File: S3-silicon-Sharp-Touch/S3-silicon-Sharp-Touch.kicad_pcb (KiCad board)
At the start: 4 copper layers, 77.9 x 45.2 mm, 66 parts, among them IC1 ESP32-S3FN8, J1 USB_C_Receptacle_USB2.0, J2 Conn_01x06_Socket, J3 Conn_01x11_Socket, J4 SM04B-SRSS-TB_LF__SN_, J5 FH52-10S-0.5SH_99, J6 5024260810, J7 S2B-PH-SM4-TB_LF__SN_, Q1 MMBT3904, Q2 MMBT3904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

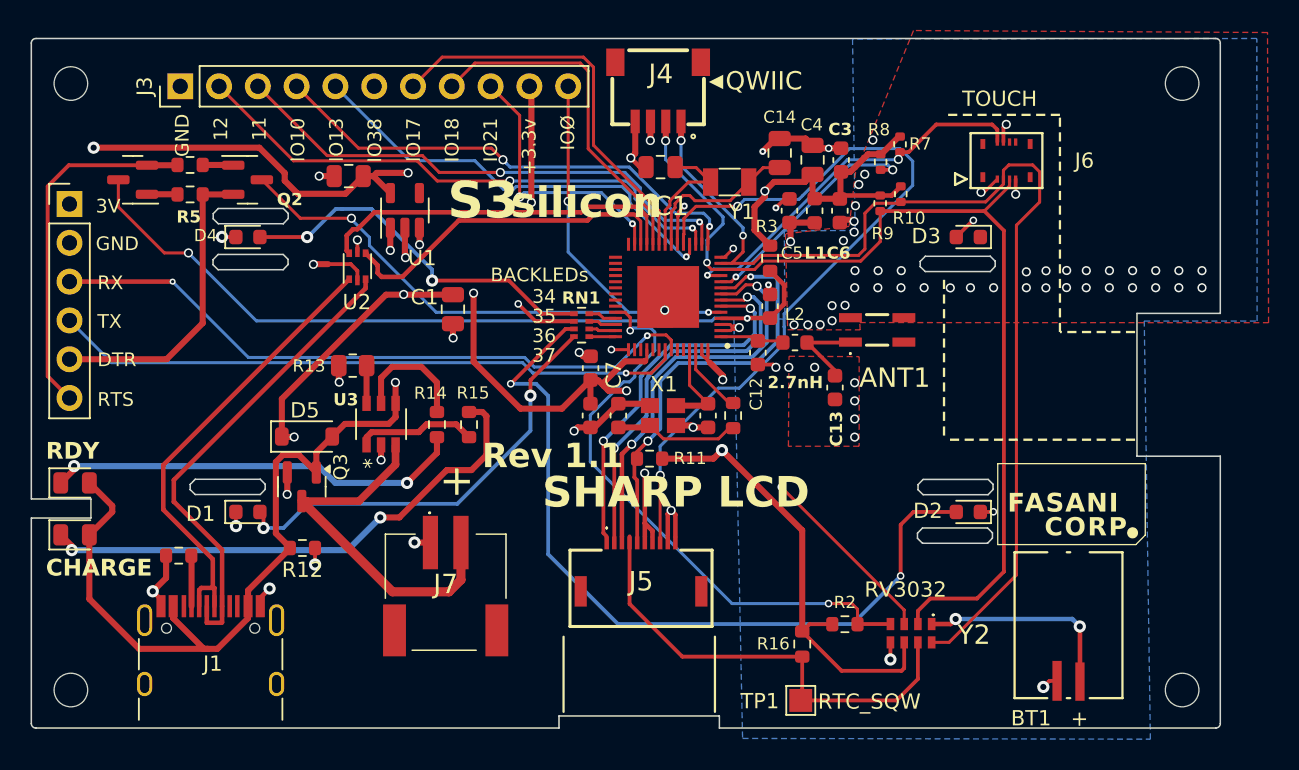
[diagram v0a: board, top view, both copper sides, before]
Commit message: Add U4:Accelerometer
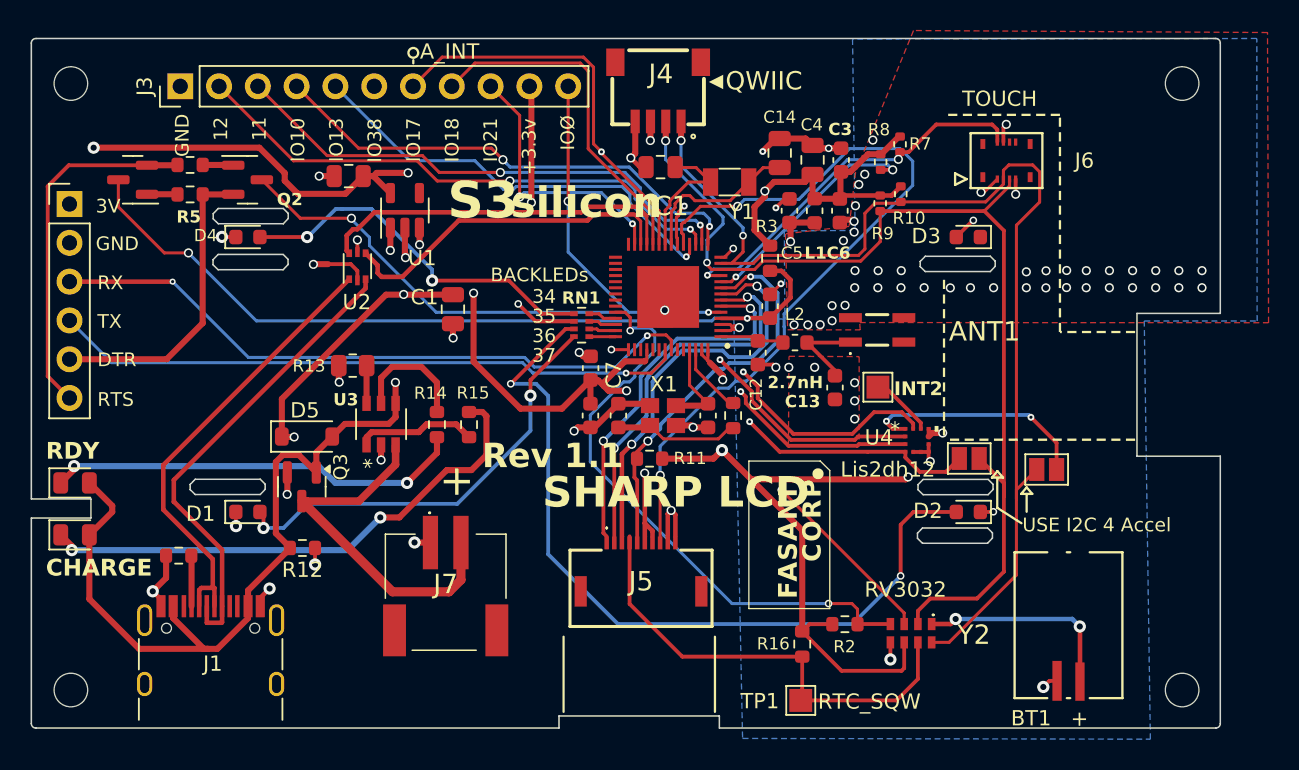
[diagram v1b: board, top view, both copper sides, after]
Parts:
- added JP1: Jumper SDA, Jumper:SolderJumper-2_P1.3mm_Open_Pad1.0x1.5mm, F.Cu at (89.1, 58.5)
- added JP2: Jumper SCL, Jumper:SolderJumper-2_P1.3mm_Open_Pad1.0x1.5mm, F.Cu at (94.1, 59.2)
- added TP2: RTC_INT, TestPoint:TestPoint_Pad_1.5x1.5mm, F.Cu at (83.1, 53.8)
- added U4: LIS2DH12TR, footprints:LIS2DH12TR_LGA-12_STM_Accel, F.Cu at (85.6, 57.3)
- moved G*** 11.0 mm to (66.6, 48.7)
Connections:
- net /IO10 renamed /A_SPI_MOSI
- net /IO11 renamed /A_SPI_CS
- net /IO13 renamed /A_SPI_MISO
- net /IO17 renamed /A_SPI_INT1
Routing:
- net /A_SPI_INT1: track 26.3 -> 63.0 mm, vias 0 -> 2
- net /A_SPI_MOSI: track 32.5 -> 66.4 mm, vias 2 -> 3
- net /A_SPI_CS: track 34.5 -> 58.8 mm, vias 2 -> 3
- net /A_SPI_MISO: track 29.0 -> 52.6 mm, vias 1 -> 2
- net VDD33: track 191.5 -> 207.8 mm, vias 11 -> 13
- net Net-(JP2-B): track 0.00 -> 15.3 mm, vias 0 -> 2
- net Net-(U4-INT2): track 0.00 -> 4.16 mm
- net /SDA: track 67.1 -> 70.2 mm
- net GND: track 49.4 -> 51.9 mm
- net /SCL: track 71.2 -> 73.7 mm
- net /LCD_DISPON: track 27.8 -> 25.6 mm
- net /CHIP_PU: track 53.5 -> 54.3 mm
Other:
- board text added: "A_INT"
- board text added: "INT2"
- board text added: "Lis2dh12"
- board text added: "TOUCH BITCH IO - - - - - 7 SCL I2C 8 SDA I2C 5 REST 6 IRQ (Int)"
- board text added: "USE I2C 4 Accel"
- board text removed: "TOUCH BITCH IO - - - - - 7 SCL I2C 8 SDA I2C 5 REST 6 IRQ (Interrupt)"

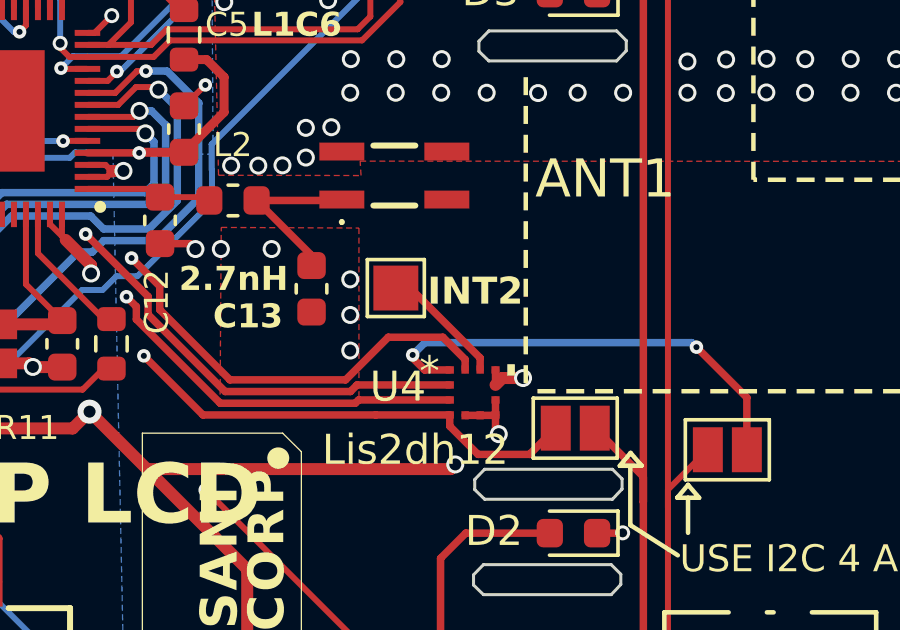
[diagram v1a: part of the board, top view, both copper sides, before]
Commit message: Add pullup to int1 (Accel)
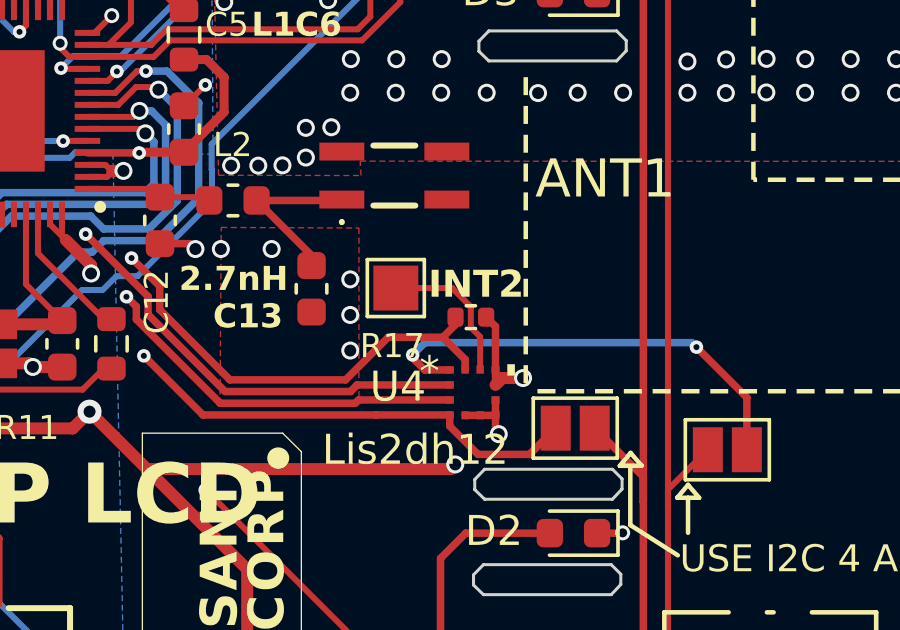
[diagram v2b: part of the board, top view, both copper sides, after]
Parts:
- added R17: 100k, Resistor_SMD:R_0402_1005Metric, F.Cu at (85.6, 54.8)
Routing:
- net VDD33: track 207.8 -> 209.6 mm
- net Net-(U4-INT2): track 4.16 -> 4.98 mm
- net /A_SPI_INT1: track 63.0 -> 63.6 mm
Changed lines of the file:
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@@
       (net 91 "Net-(JP2-B)") (pinfunction "B") (pintype "passive"))
   )
+  (footprint "Resistor_SMD:R_0402_1005Metric" (layer "F.Cu")
+    (at 85.58 54.8)
+    (descr "Resistor SMD 0402 (1005 Metric), square (rectangular) end terminal, IPC_7351 nominal, (Body size source: IPC-SM-782 page 72, https://www.pcb-3d.com/wordpress/wp-content/uploads/ipc-sm-782a_amendment_1_and_2.pdf), generated with kicad-footprint-generator")
+    (tags "resistor")
+    (property "LCSC" "C208960")
+    (property "Sheetfile" "S3-silicon-Sharp-Touch.kicad_sch")
+    (property "Sheetname" "")
+    (property "ki_description" "Resistor")
+    (property "ki_keywords" "R res resistor")
+    (attr smd)
+    (fp_text reference "R17" (at -2.62 0.96) (layer "F.SilkS")
+        (effects (font (size 0.8 0.8) (thickness 0.15)))
+    )
+    (fp_text value "100k" (at 0 1.17) (layer "F.Fab")
+        (effects (font (size 1 1) (thickness 0.15)))
+    )
+    (fp_text user "${REFERENCE}" (at 0 0) (layer "F.Fab")
+        (effects (font (size 0.26 0.26) (thickness 0.04)))
+    )
+    (fp_line (start -0.153641 -0.38) (end 0.153641 -0.38)
+      (stroke (width 0.12) (type solid)) (layer "F.SilkS"))
+    (fp_line (start -0.153641 0.38) (end 0.153641 0.38)
+      (stroke (width 0.12) (type solid)) (layer "F.SilkS"))
+    (fp_line (start -0.93 -0.47) (end 0.93 -0.47)
+      (stroke (width 0.05) (type solid)) (layer "F.CrtYd"))
+    (fp_line (start -0.93 0.47) (end -0.93 -0.47)
+      (stroke (width 0.05) (type solid)) (layer "F.CrtYd"))
+    (fp_line (start 0.93 -0.47) (end 0.93 0.47)
+      (stroke (width 0.05) (type solid)) (layer "F.CrtYd"))
+    (fp_line (start 0.93 0.47) (end -0.93 0.47)
+      (stroke (width 0.05) (type solid)) (layer "F.CrtYd"))
+    (fp_line (start -0.525 -0.27) (end 0.525 -0.27)
+      (stroke (width 0.1) (type solid)) (layer "F.Fab"))
+    (fp_line (start -0.525 0.27) (end -0.525 -0.27)
+      (stroke (width 0.1) (type solid)) (layer "F.Fab"))
+    (fp_line (start 0.525 -0.27) (end 0.525 0.27)
+      (stroke (width 0.1) (type solid)) (layer "F.Fab"))
+    (fp_line (start 0.525 0.27) (end -0.525 0.27)
+      (stroke (width 0.1) (type solid)) (layer "F.Fab"))
+    (pad "1" smd roundrect (at -0.51 0) (size 0.54 0.64) (layers "F.Cu" "F.Paste" "F.Mask") (roundrect_rratio 0.25)
+      (net 95 "/A_SPI_INT1") (pintype "passive"))
+    (pad "2" smd roundrect (at 0.51 0) (size 0.54 0.64) (layers "F.Cu" "F.Paste" "F.Mask") (roundrect_rratio 0.25)
+      (net 3 "VDD33") (pintype "passive"))
+    (model "${KICAD6_3DMODEL_DIR}/Resistor_SMD.3dshapes/R_0402_1005Metric.wrl"
+      (offset (xyz 0 0 0))
+      (scale (xyz 1 1 1))
+      (rotate (xyz 0 0 0))
+    )
+  )
   (footprint "foot_sharp:QWIIC_SM04B-SRSS-TB_LFSN_" (layer "F.Cu")
     (at 71.69 31.770315 180)
@@
     (effects (font (size 1 1) (thickness 0.15)))
   )
-  (gr_text "INT2" (at 84.13 54.46) (layer "F.SilkS")
+  (gr_text "INT2" (at 84.16 54.23) (layer "F.SilkS")
     (effects (font (size 0.9 0.9) (thickness 0.18) bold) (justify left bottom))
   )
@@
   (segment (start 87.32 56.83) (end 86.6325 56.83) (width 0.4) (layer "F.Cu") (net 3))
   (segment (start 64.27 53.36) (end 64.68 53.36) (width 0.4) (layer "F.Cu") (net 3))
+  (segment (start 86.4025 56.559999) (end 86.4025 55.1125) (width 0.25) (layer "F.Cu") (net 3))
   (segment (start 64.77 53.39) (end 65.13 53.75) (width 0.4) (layer "F.Cu") (net 3))
   (segment (start 71.55 51.7) (end 72.075 52.225) (width 0.2) (layer "F.Cu") (net 3))
@@
   (segment (start 72.31 58.51) (end 68.955 58.51) (width 0.4) (layer "F.Cu") (net 3))
   (segment (start 80.67 39.735) (end 81.275 39.735) (width 0.4) (layer "F.Cu") (net 3))
+  (segment (start 86.4025 55.1125) (end 86.09 54.8) (width 0.25) (layer "F.Cu") (net 3))
   (segment (start 67.81 52.14) (end 67.85 52.1) (width 0.4) (layer "F.Cu") (net 3))
   (segment (start 78.8 41.3525) (end 78.94 41.4925) (width 0.4) (layer "F.Cu") (net 3))
@@
   (segment (start 83.64 56.06) (end 84.05 55.65) (width 0.25) (layer "B.Cu") (net 91))
   (segment (start 92.95 55.65) (end 93.1 55.8) (width 0.25) (layer "B.Cu") (net 91))
-  (segment (start 85.89 56.16) (end 83.56 53.83) (width 0.25) (layer "F.Cu") (net 92))
-  (segment (start 85.89 56.5475) (end 85.89 56.16) (width 0.25) (layer "F.Cu") (net 92))
-  (segment (start 83.56 53.83) (end 83.08 53.83) (width 0.25) (layer "F.Cu") (net 92))
+  (segment (start 85.89 56.5475) (end 85.89 55.454072) (width 0.2) (layer "F.Cu") (net 92))
+  (segment (start 85.89 55.454072) (end 85.58 55.144072) (width 0.2) (layer "F.Cu") (net 92))
+  (segment (start 85.58 55.144072) (end 85.58 54.455928) (width 0.2) (layer "F.Cu") (net 92))
+  (segment (start 84.954072 53.83) (end 83.08 53.83) (width 0.2) (layer "F.Cu") (net 92))
+  (segment (start 85.58 54.455928) (end 84.954072 53.83) (width 0.2) (layer "F.Cu") (net 92))
   (segment (start 53.26 38.67) (end 47.02 38.67) (width 0.2) (layer "F.Cu") (net 93))
   (segment (start 84.8775 57.06) (end 81.786911 57.06) (width 0.25) (layer "F.Cu") (net 93))
@@
   (segment (start 81.405363 56.890004) (end 77.550004 56.890004) (width 0.25) (layer "F.Cu") (net 95))
   (segment (start 85.39 56.5475) (end 85.39 56.211544) (width 0.25) (layer "F.Cu") (net 95))
+  (segment (start 85.07 55.048456) (end 84.648456 55.47) (width 0.25) (layer "F.Cu") (net 95))
   (segment (start 54.55 32.22) (end 63.8 32.22) (width 0.2) (layer "F.Cu") (net 95))
   (segment (start 63.8 32.22) (end 64.46 32.88) (width 0.2) (layer "F.Cu") (net 95))
   (segment (start 52.64 34.13) (end 54.55 32.22) (width 0.2) (layer "F.Cu") (net 95))
   (segment (start 77.550004 56.890004) (end 75.21 54.55) (width 0.25) (layer "F.Cu") (net 95))
-  (segment (start 85.39 56.211544) (end 84.648456 55.47) (width 0.25) (layer "F.Cu") (net 95))
   (segment (start 82.825367 55.47) (end 81.405363 56.890004) (width 0.25) (layer "F.Cu") (net 95))
   (segment (start 68.75 42.28) (end 64.98 38.51) (width 0.2) (layer "F.Cu") (net 95))
@@
   (segment (start 75.21 54.55) (end 75.21 53.77) (width 0.25) (layer "F.Cu") (net 95))
   (segment (start 68.75 42.28) (end 68.75 44.475) (width 0.2) (layer "F.Cu") (net 95))
+  (segment (start 84.648456 55.47) (end 85.39 56.211544) (width 0.25) (layer "F.Cu") (net 95))
   (segment (start 64.98 38.42) (end 64.89 38.42) (width 0.25) (layer "F.Cu") (net 95))
   (segment (start 84.648456 55.47) (end 82.825367 55.47) (width 0.25) (layer "F.Cu") (net 95))

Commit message: Update INT1 to be pull-down
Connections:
- R17 pad 2: VDD33 -> GND
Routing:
- net Net-(U4-INT2): track 4.98 -> 7.52 mm
- net VDD33: track 209.6 -> 207.8 mm
- net GND: track 51.9 -> 52.6 mm, vias 74 -> 75
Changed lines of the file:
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@@
       (net 95 "/A_SPI_INT1") (pintype "passive"))
     (pad "2" smd roundrect (at 0.51 0) (size 0.54 0.64) (layers "F.Cu" "F.Paste" "F.Mask") (roundrect_rratio 0.25)
-      (net 3 "VDD33") (pintype "passive"))
+      (net 2 "GND") (pintype "passive"))
     (model "${KICAD6_3DMODEL_DIR}/Resistor_SMD.3dshapes/R_0402_1005Metric.wrl"
       (offset (xyz 0 0 0))
@@
   (segment (start 51.49 53.52) (end 51.49 51.06) (width 0.4) (layer "In2.Cu") (net 1))
   (segment (start 79.86 38.19) (end 79.865 38.185) (width 0.4) (layer "F.Cu") (net 2))
+  (segment (start 86.8 54.8) (end 86.81 54.79) (width 0.25) (layer "F.Cu") (net 2))
   (segment (start 90.63 62) (end 90.64 61.99) (width 0.25) (layer "F.Cu") (net 2))
   (segment (start 78.35 37.55) (end 78.8 38) (width 0.4) (layer "F.Cu") (net 2))
@@
   (segment (start 80.625 42.865) (end 81.41125 42.865) (width 0.4) (layer "F.Cu") (net 2))
   (segment (start 64.27 51.81) (end 63.780662 51.81) (width 0.4) (layer "F.Cu") (net 2))
+  (segment (start 86.09 54.8) (end 86.8 54.8) (width 0.25) (layer "F.Cu") (net 2))
   (segment (start 76.02 47.755) (end 76.008978 47.755) (width 0.2) (layer "F.Cu") (net 2))
   (segment (start 48.565 45.775) (end 47.08 45.775) (width 0.25) (layer "F.Cu") (net 2))
@@
   (via (at 76.73 47.06) (size 0.45) (drill 0.2) (layers "F.Cu" "B.Cu") (net 2))
   (via (at 91.486956 36.623686) (size 0.6) (drill 0.4) (layers "F.Cu" "B.Cu") (net 2))
+  (via (at 86.81 54.79) (size 0.5) (drill 0.3) (layers "F.Cu" "B.Cu") (net 2))
   (via (at 52.74 64) (size 0.8) (drill 0.4) (layers "F.Cu" "B.Cu") (net 2))
   (via (at 98.241326 46.2) (size 0.6) (drill 0.4) (layers "F.Cu" "B.Cu") (free) (net 2))
@@
   (segment (start 87.32 56.83) (end 86.6325 56.83) (width 0.4) (layer "F.Cu") (net 3))
   (segment (start 64.27 53.36) (end 64.68 53.36) (width 0.4) (layer "F.Cu") (net 3))
-  (segment (start 86.4025 56.559999) (end 86.4025 55.1125) (width 0.25) (layer "F.Cu") (net 3))
   (segment (start 64.77 53.39) (end 65.13 53.75) (width 0.4) (layer "F.Cu") (net 3))
   (segment (start 71.55 51.7) (end 72.075 52.225) (width 0.2) (layer "F.Cu") (net 3))
@@
   (segment (start 72.31 58.51) (end 68.955 58.51) (width 0.4) (layer "F.Cu") (net 3))
   (segment (start 80.67 39.735) (end 81.275 39.735) (width 0.4) (layer "F.Cu") (net 3))
-  (segment (start 86.4025 55.1125) (end 86.09 54.8) (width 0.25) (layer "F.Cu") (net 3))
   (segment (start 67.81 52.14) (end 67.85 52.1) (width 0.4) (layer "F.Cu") (net 3))
   (segment (start 78.8 41.3525) (end 78.94 41.4925) (width 0.4) (layer "F.Cu") (net 3))
@@
   (segment (start 83.64 56.06) (end 84.05 55.65) (width 0.25) (layer "B.Cu") (net 91))
   (segment (start 92.95 55.65) (end 93.1 55.8) (width 0.25) (layer "B.Cu") (net 91))
-  (segment (start 85.89 56.5475) (end 85.89 55.454072) (width 0.2) (layer "F.Cu") (net 92))
-  (segment (start 85.89 55.454072) (end 85.58 55.144072) (width 0.2) (layer "F.Cu") (net 92))
-  (segment (start 85.58 55.144072) (end 85.58 54.455928) (width 0.2) (layer "F.Cu") (net 92))
-  (segment (start 84.954072 53.83) (end 83.08 53.83) (width 0.2) (layer "F.Cu") (net 92))
-  (segment (start 85.58 54.455928) (end 84.954072 53.83) (width 0.2) (layer "F.Cu") (net 92))
+  (segment (start 86.49 55.57) (end 87.04 55.57) (width 0.25) (layer "F.Cu") (net 92))
+  (segment (start 87.41 55.2) (end 87.41 54.647537) (width 0.25) (layer "F.Cu") (net 92))
+  (segment (start 85.89 56.17) (end 86.49 55.57) (width 0.25) (layer "F.Cu") (net 92))
+  (segment (start 86.592463 53.83) (end 83.08 53.83) (width 0.25) (layer "F.Cu") (net 92))
+  (segment (start 85.89 56.5475) (end 85.89 56.17) (width 0.25) (layer "F.Cu") (net 92))
+  (segment (start 87.04 55.57) (end 87.41 55.2) (width 0.25) (layer "F.Cu") (net 92))
+  (segment (start 87.41 54.647537) (end 86.592463 53.83) (width 0.25) (layer "F.Cu") (net 92))
   (segment (start 53.26 38.67) (end 47.02 38.67) (width 0.2) (layer "F.Cu") (net 93))
   (segment (start 84.8775 57.06) (end 81.786911 57.06) (width 0.25) (layer "F.Cu") (net 93))
